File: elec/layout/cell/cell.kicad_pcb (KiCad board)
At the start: 4 copper layers, 55 parts

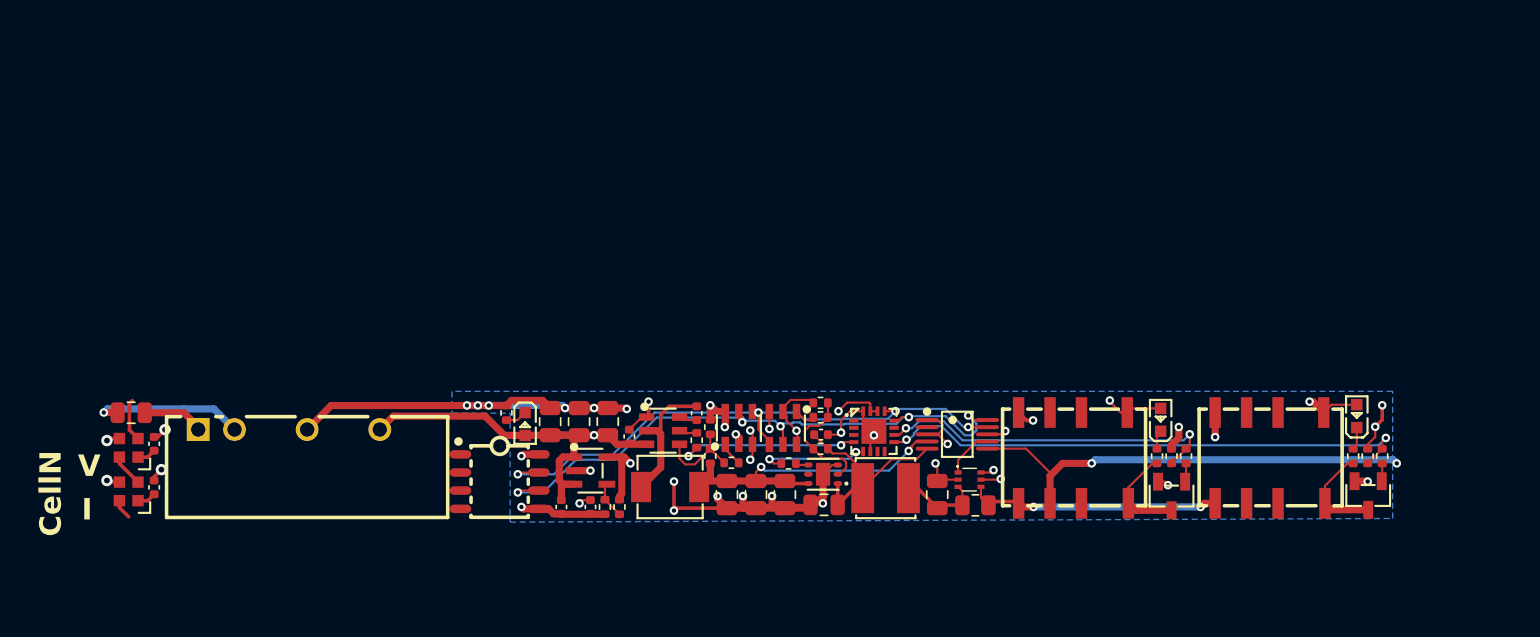
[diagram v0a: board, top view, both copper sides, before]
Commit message: merge firmware and layout from BMS project
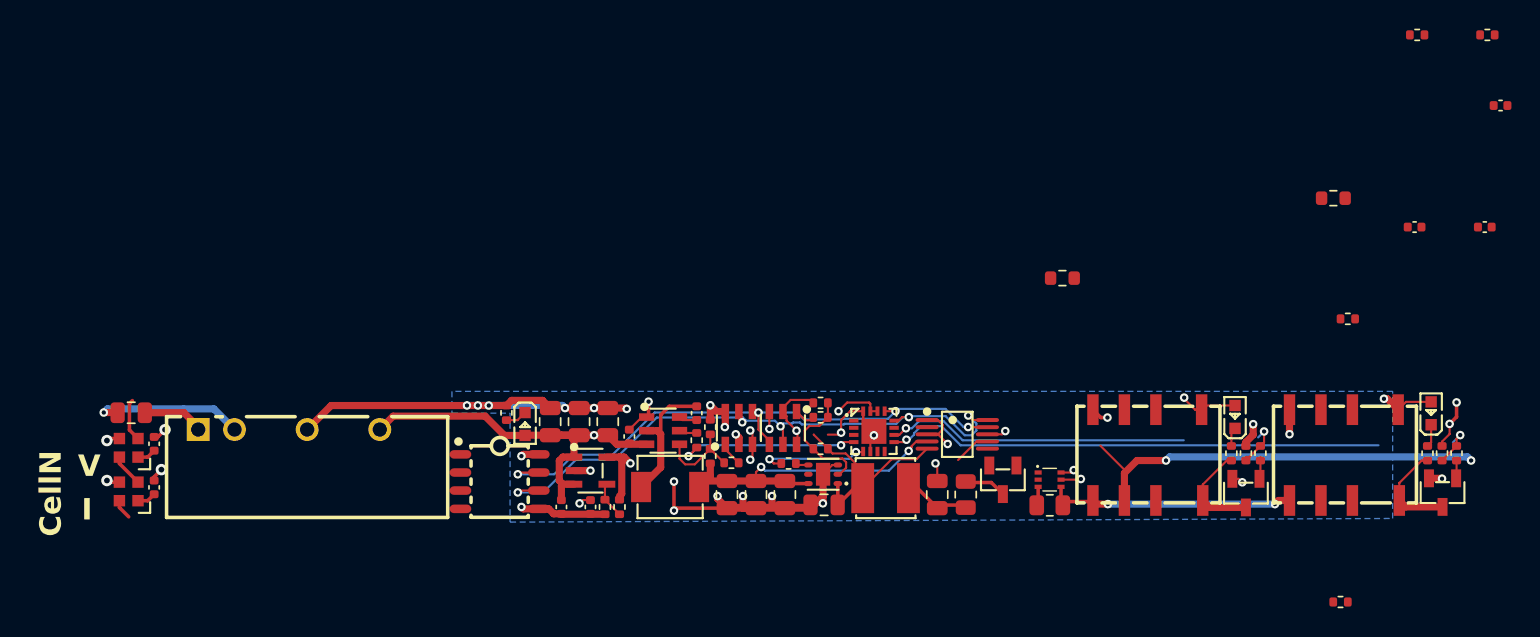
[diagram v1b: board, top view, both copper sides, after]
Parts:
- added C11: 16V 100nF X7R ±10% 0402 Multilayer Ceramic Capacitors MLCC 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, lib:C0402, F.Cu at (152.5, 104.3)
- added C12: 50V 10nF X7R ±10% 0402 Multilayer Ceramic Capacitors MLCC -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, lib:C0402, F.Cu at (147.6, 104.3)
- added Q3: ?, lib:SOT-23-3_L2.9-W1.3-P1.90-LS2.4-BR, F.Cu at (118.8, 122.0)
- added R17: 100mW Thick Film Resistors 75V ±100ppm/℃ ±1% 1kΩ 0603 Chip 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, lib:R0603, F.Cu at (123.0, 107.9)
- added R18: 100mW Thick Film Resistors 75V ±100ppm/℃ ±1% 10kΩ 0603 Chip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, lib:R0603, F.Cu at (141.9, 102.3)
- added R19: 125mW Thick Film Resistors 150V ±100ppm/℃ ±1% 226Ω 0805 Chi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, lib:R0805, F.Cu at (116.2, 123.0)
- added R20: 62.5mW Thick Film Resistors 50V ±100ppm/℃ ±1% 10kΩ 0402 Chi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, lib:R0402, F.Cu at (147.8, 90.9)
- added R21: 62.5mW Thick Film Resistors 50V ±100ppm/℃ ±1% 10kΩ 0402 Chi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, lib:R0402, F.Cu at (152.7, 90.9)
- added R24: 62.5mW Thick Film Resistors 50V ±100ppm/℃ ±1% 10kΩ 0402 Chi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, lib:R0402, F.Cu at (142.4, 130.6)
- added R25: 62.5mW Thick Film Resistors 50V ±100ppm/℃ ±1% 10kΩ 0402 Chi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, lib:R0402, F.Cu at (142.9, 110.8)
- C10: value 25V 1uF X5R ±10% 0402 Multilayer Ceramic Capacitors MLCC - SMD/SMT ROHS -> 25V 1uF X5R ±10% 0402 Multilayer Ceramic Capacitors MLCC - SMD/SMT ROHS
- C13: renamed from C11; value 25V 10uF X5R ±10% 0805 Multilayer Ceramic Capacitors MLCC - SMD/SMT ROHS -> 25V 10uF X5R ±10% 0805 Multilayer Ceramic Capacitors MLCC - SMD/SMT ROHS
- C14: renamed from C12; value 25V 10uF X5R ±10% 0805 Multilayer Ceramic Capacitors MLCC - SMD/SMT ROHS -> 25V 10uF X5R ±10% 0805 Multilayer Ceramic Capacitors MLCC - SMD/SMT ROHS
- C15: renamed from C13; value 16V 100nF X7R ±10% 0402 Multilayer Ceramic Capacitors MLCC - SMD/SMT ROHS -> 16V 100nF X7R ±10% 0402 Multilayer Ceramic Capacitors MLCC - SMD/SMT ROHS
- C16: renamed from C14; value 16V 100nF X7R ±10% 0402 Multilayer Ceramic Capacitors MLCC - SMD/SMT ROHS -> 16V 100nF X7R ±10% 0402 Multilayer Ceramic Capacitors MLCC - SMD/SMT ROHS
- C17: renamed from C15; value 25V 1uF X5R ±10% 0402 Multilayer Ceramic Capacitors MLCC - SMD/SMT ROHS -> 25V 1uF X5R ±10% 0402 Multilayer Ceramic Capacitors MLCC - SMD/SMT ROHS
- C18: renamed from C16; value 25V 1uF X5R ±10% 0402 Multilayer Ceramic Capacitors MLCC - SMD/SMT ROHS -> 25V 1uF X5R ±10% 0402 Multilayer Ceramic Capacitors MLCC - SMD/SMT ROHS
- C2, C3, C4, C6, C7, C8: value 25V 10uF X5R ±10% 0805 Multilayer Ceramic Capacitors MLCC - SMD/SMT ROHS -> 25V 10uF X5R ±10% 0805 Multilayer Ceramic Capacitors MLCC - SMD/SMT ROHS
- C5, C9: value 16V 100nF X7R ±10% 0402 Multilayer Ceramic Capacitors MLCC - SMD/SMT ROHS -> 16V 100nF X7R ±10% 0402 Multilayer Ceramic Capacitors MLCC - SMD/SMT ROHS
- L1, LED1, LED2, LED3, Q1, Q2, U1, U10, U11, U12, U13, U14, U2, U3, U4, U5, U6, U7, U8, U9: value (none) -> ?
- L2: value 100uH -> ?
- R1: value 62.5mW Thick Film Resistors 50V ±100ppm/℃ ±1% 21kΩ 0402 Chip Resistor - Surface Mount ROHS -> 62.5mW Thick Film Resistors 50V ±100ppm/℃ ±1% 14kΩ 0402 Chip Resistor - Surface Mount ROHS
- R10: value 125mW Thick Film Resistors ±600ppm/℃ ±1% 110mΩ 0805 Chip Resistor - Surface Mount ROHS -> 125mW Thick Film Resistors 150V ±1% 100mΩ 0805 Chip Resistor - Surface Mount ROHS
- R11, R14: value 62.5mW Thick Film Resistors 50V ±100ppm/℃ ±1% 21kΩ 0402 Chip Resistor - Surface Mount ROHS -> 62.5mW Thick Film Resistors 50V ±100ppm/℃ ±1% 13kΩ 0402 Chip Resistor - Surface Mount ROHS
- R12, R15, R4, R5, R8, R9: value 62.5mW Thick Film Resistors 50V ±100ppm/℃ ±1% 10kΩ 0402 Chip Resistor - Surface Mount ROHS -> 62.5mW Thick Film Resistors 50V ±100ppm/℃ ±1% 10kΩ 0402 Chip Resistor - Surface Mount ROHS
- R13, R16: value 62.5mW Thick Film Resistors 50V ±100ppm/℃ ±1% 1kΩ 0402 Chip Resistor - Surface Mount ROHS -> 62.5mW Thick Film Resistors 50V ±100ppm/℃ ±1% 1kΩ 0402 Chip Resistor - Surface Mount ROHS
- R2: value 62.5mW Thick Film Resistors 50V ±100ppm/℃ ±1% 24kΩ 0402 Chip Resistor - Surface Mount ROHS -> 62.5mW Thick Film Resistors 50V ±100ppm/℃ ±1% 24kΩ 0402 Chip Resistor - Surface Mount ROHS
- R22: renamed from R17; value 62.5mW Thick Film Resistors 50V ±100ppm/℃ ±1% 11.5kΩ 0402 Chip Resistor - Surface Mount ROHS -> 62.5mW Thick Film Resistors 50V ±100ppm/℃ ±1% 11.5kΩ 0402 Chip Resistor - Surface Mount ROHS
- R23: renamed from R18; value 62.5mW Thick Film Resistors 50V ±100ppm/℃ ±1% 6.2kΩ 0402 Chip Resistor - Surface Mount ROHS -> 62.5mW Thick Film Resistors 50V ±100ppm/℃ ±1% 6.2kΩ 0402 Chip Resistor - Surface Mount ROHS
- R3: value 62.5mW Thick Film Resistors 50V ±100ppm/℃ ±1% 37.4kΩ 0402 Chip Resistor - Surface Mount ROHS -> 62.5mW Thick Film Resistors 50V ±100ppm/℃ ±1% 37.4kΩ 0402 Chip Resistor - Surface Mount ROHS
- R6: value 62.5mW Thick Film Resistors 50V ±100ppm/℃ ±1% 43kΩ 0402 Chip Resistor - Surface Mount ROHS -> 62.5mW Thick Film Resistors 50V ±100ppm/℃ ±1% 43kΩ 0402 Chip Resistor - Surface Mount ROHS
- R7: value 62.5mW Thick Film Resistors 50V ±100ppm/℃ ±1% 59kΩ 0402 Chip Resistor - Surface Mount ROHS -> 62.5mW Thick Film Resistors 50V ±100ppm/℃ ±1% 60.4kΩ 0402 Chip Resistor - Surface Mount ROHS
- moved C10 52.8 mm to (153.6, 95.8)
- moved U7 5.60 mm to (122.1, 122.0)
- moved LED3 5.20 mm to (148.7, 117.4)
- moved Q2 5.20 mm to (149.5, 122.9)
- moved R11 5.20 mm to (134.8, 120.2)
- moved R16 5.20 mm to (149.5, 120.2)
- moved U9 5.20 mm to (142.7, 120.3)
- moved LED2 5.20 mm to (135.0, 117.6)
- moved Q1 5.20 mm to (135.8, 122.9)
- moved R12 5.20 mm to (136.8, 120.2)
- moved R13 5.20 mm to (135.8, 120.2)
- moved R14 5.20 mm to (148.5, 120.2)
- moved R15 5.20 mm to (150.5, 120.2)
- moved U8 5.20 mm to (128.9, 120.3)
- moved R10 5.20 mm to (122.1, 123.8)
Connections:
- net int_hash renamed int
- LED3 pad 2: vcc-6 -> vcc-2
- Q2 pad 2: gnd-6 -> gnd-2
- R12 pad 1: output_relay-input -> input
- R13 pad 1: output_relay-input -> input
- R15 pad 1: dmm_relay-input -> dmm_relay_enable
- R16 pad 1: dmm_relay-input -> dmm_relay_enable
- R16 pad 2: gnd-6 -> gnd-2
- U10 pad 1: reset_hash -> vcc-7
- U10 pad 10: output_relay-input -> p7
- U10 pad 9: dmm_relay-input -> p6
- U3 pad 6: gnd-6 -> vcc-6
- U9 pad 1: vcc-6 -> vcc-2
- U9 pad 3: gnd-4 -> dmm_relay-gnd
- U9 pad 6: vcc-4 -> dmm_relay-vcc
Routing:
- net dmm_relay-input: track 38.0 -> 0.00 mm, vias 2 -> 0
- net p6: track 0.00 -> 35.0 mm, vias 0 -> 1
- net output_relay-input: track 24.4 -> 0.00 mm, vias 2 -> 0
- net p7: track 0.00 -> 21.4 mm, vias 0 -> 1
- net gnd-6: track 106.6 -> 100.9 mm, vias 31 -> 29
- net gnd-2: track 3.80 -> 8.19 mm, vias 4 -> 6
- net input: track 0.00 -> 3.04 mm, vias 0 -> 1
- net dmm_relay_enable: track 0.00 -> 3.03 mm, vias 0 -> 1
- net n: track 0.00 -> 2.96 mm
- net vcc-1: track 34.0 -> 31.3 mm
- net ain3: track 3.47 -> 2.59 mm
